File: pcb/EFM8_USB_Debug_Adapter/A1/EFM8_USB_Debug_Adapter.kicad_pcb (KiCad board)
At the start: 2 copper layers, 27 parts, among them J100 EFM8 IDC Debug Header, J101 Conn_01x06, J110 2137160001, J120 31230102, J130 EFM8 USB 8-Bit Debug Header, J131 Conn_01x02_Male, Q110 SI3443CDV-T1-GE3, Q111 DMMT5401, Q120 SI3443CDV-T1-GE3, Q121 DMMT5401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

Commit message: Erstes Layout
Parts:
- removed J101: Conn_01x06, Connector_PinHeader_2.54mm:PinHeader_1x06_P2.54mm_Vertical
- added J111: TTL-232R Header, Connector_PinHeader_2.54mm:PinHeader_1x06_P2.54mm_Vertical, F.Cu at (142.2, 34.3)
- moved D110 47.6 mm to (110.5, 34.3), turned to 180 degrees
- moved R112 47.3 mm to (114.0, 35.0), turned to -90 degrees
- moved R110 45.9 mm to (110.5, 36.8)
- moved F110 44.3 mm to (110.5, 41.9)
- moved R111 43.8 mm to (110.5, 39.4)
- moved D120 39.8 mm to (131.7, 33.9), turned to 90 degrees
- moved R130 38.6 mm to (110.5, 63.5)
- moved J110 38.0 mm to (105.1, 35.1), turned to -90 degrees
- moved R114 33.0 mm to (109.2, 51.0), turned to -90 degrees
- moved R113 31.8 mm to (116.8, 51.0), turned to 90 degrees
- moved Q110 29.9 mm to (111.0, 46.0)
- moved R121 29.3 mm to (124.0, 49.2), turned to 90 degrees
- moved Q111 28.1 mm to (113.0, 51.0), turned to 180 degrees
- moved R120 26.9 mm to (131.7, 39.0), turned to -90 degrees
- moved J131 24.3 mm to (114.3, 58.4), turned to 90 degrees
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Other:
- board outline added: 48 x 35 mm

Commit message: PCB bearbeitet, FreeCAD Projet angelegt
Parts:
- removed J131: Conn_01x02_Male, Connector_PinHeader_2.54mm:PinHeader_1x02_P2.54mm_Vertical
- added D111: 150080SS75000, LED_SMD:LED_0805_2012Metric_Pad1.15x1.40mm_HandSolder, F.Cu at (98.8, 46.8)
- added D121: 150080SS75000, LED_SMD:LED_0805_2012Metric_Pad1.15x1.40mm_HandSolder, F.Cu at (127.8, 34.8)
- added D131: 150080BS75000, LED_SMD:LED_0805_2012Metric_Pad1.15x1.40mm_HandSolder, F.Cu at (98.8, 74.2)
- added JP130: SolderJumper_2_Bridged, Jumper:SolderJumper-2_P1.3mm_Bridged_RoundedPad1.0x1.5mm, F.Cu at (114.0, 58.4)
- added R115: 2k,0603, Resistor_SMD:R_0603_1608Metric_Pad0.98x0.95mm_HandSolder, F.Cu at (107.6, 47.6)
- added R123: 2k,0603, Resistor_SMD:R_0603_1608Metric_Pad0.98x0.95mm_HandSolder, F.Cu at (129.0, 46.8)
- added R133: 2k,0603, Resistor_SMD:R_0603_1608Metric_Pad0.98x0.95mm_HandSolder, F.Cu at (113.2, 67.0)
- D110, D120: value LTST-C191TGKT -> 150080SS75000; footprint LED_SMD:LED_0603_1608Metric_Pad1.05x0.95mm_HandSolder -> LED_SMD:LED_0805_2012Metric_Pad1.15x1.40mm_HandSolder
- D130: value LTST-C191TGKT -> 150080BS75000; footprint LED_SMD:LED_0603_1608Metric_Pad1.05x0.95mm_HandSolder -> LED_SMD:LED_0805_2012Metric_Pad1.15x1.40mm_HandSolder
- F110: value 0805L110SLxx -> 0ZCJ0110FF2E; footprint Fuse:Fuse_0805_2012Metric_Pad1.15x1.40mm_HandSolder -> Fuse:Fuse_1206_3216Metric_Pad1.42x1.75mm_HandSolder
- J100: value EFM8 IDC Debug Header -> EFM8_IDC_Debug_Header_Horizontal; footprint Connector_User:IDC-Header_2x03_P2.54mm_Vertical_61200621621 -> Connector_User:IDC-Header_2x03_P2.54mm_Horizontal_61200621721
- J111: value TTL-232R Header -> TTL-232R_Header_Horizontal; footprint Connector_PinHeader_2.54mm:PinHeader_1x06_P2.54mm_Vertical -> Connector_PinHeader_2.54mm:PinHeader_1x06_P2.54mm_Horizontal
- J130: value EFM8 USB 8-Bit Debug Header -> EFM8_USB_8-Bit_Debug_Header_Horizontal; footprint Connector_User:IDC-Header_2x05_P2.54mm_Vertical_61201021621 -> Connector_User:IDC-Header_2x05_P2.54mm_Horizontal_61201021721
- moved R120 20.8 mm to (111.0, 40.6)
- moved D120 19.5 mm to (112.2, 34.8)
- moved D130 19.5 mm to (98.8, 50.4)
- moved J130 18.6 mm to (108.8, 67.4), turned to 180 degrees
- moved R122 14.4 mm to (118.6, 46.8), turned to -90 degrees
- moved R130 14.0 mm to (107.6, 49.8)
- moved D110 11.7 mm to (98.8, 34.0)
- moved Q120 11.4 mm to (125.2, 52.4)
- moved Q110 10.9 mm to (119.8, 52.4)
- moved R112 7.20 mm to (106.8, 34.8)
- moved Q131 6.56 mm to (117.0, 62.6)
- moved R131 6.56 mm to (120.8, 62.6)
- moved R132 6.56 mm to (113.2, 62.6)
- moved J100 6.48 mm to (134.2, 59.3), turned to 0 degrees
- moved R114 6.24 mm to (113.8, 55.2), turned to 0 degrees
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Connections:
- net Net-(D110-Pad2) renamed /Ext_USB_Power_Fused
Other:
- board size 48 x 35 mm -> 51 x 44 mm

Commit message: Mechanik bearbeitet
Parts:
- moved D121 4.00 mm to (131.8, 34.8)
- moved D120 4.00 mm to (116.2, 34.8)
- moved J100 4.00 mm to (138.2, 59.3)
- moved J111 4.00 mm to (141.4, 35.6)
- moved J120 4.00 mm to (126.5, 41.4)
- moved Q121 4.00 mm to (126.8, 46.8)
- moved R121 4.00 mm to (130.6, 46.8)
- moved R122 4.00 mm to (122.6, 46.8)
- moved R123 4.00 mm to (133.0, 46.8)
- moved R110 1.20 mm to (107.8, 37.8)
- moved R115 1.20 mm to (107.6, 46.4)
- moved R120 1.20 mm to (111.0, 39.4)
- moved F110 1.20 mm to (108.4, 43.6)
- moved R111 1.20 mm to (107.8, 40.6)
- moved R112 1.20 mm to (106.8, 33.6)
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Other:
- board size 51 x 44 mm -> 55 x 45 mm

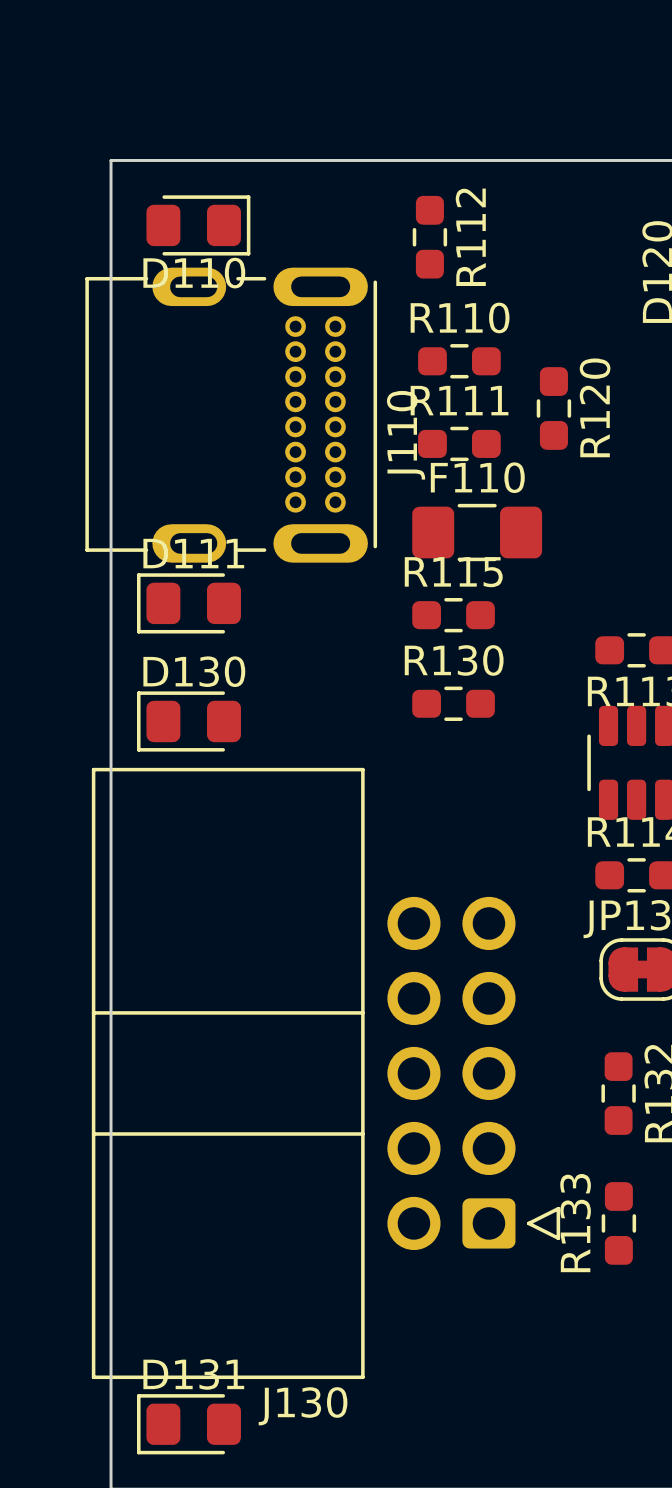
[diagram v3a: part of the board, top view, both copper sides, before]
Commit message: Light Pipes in KiCad hinzugefügt
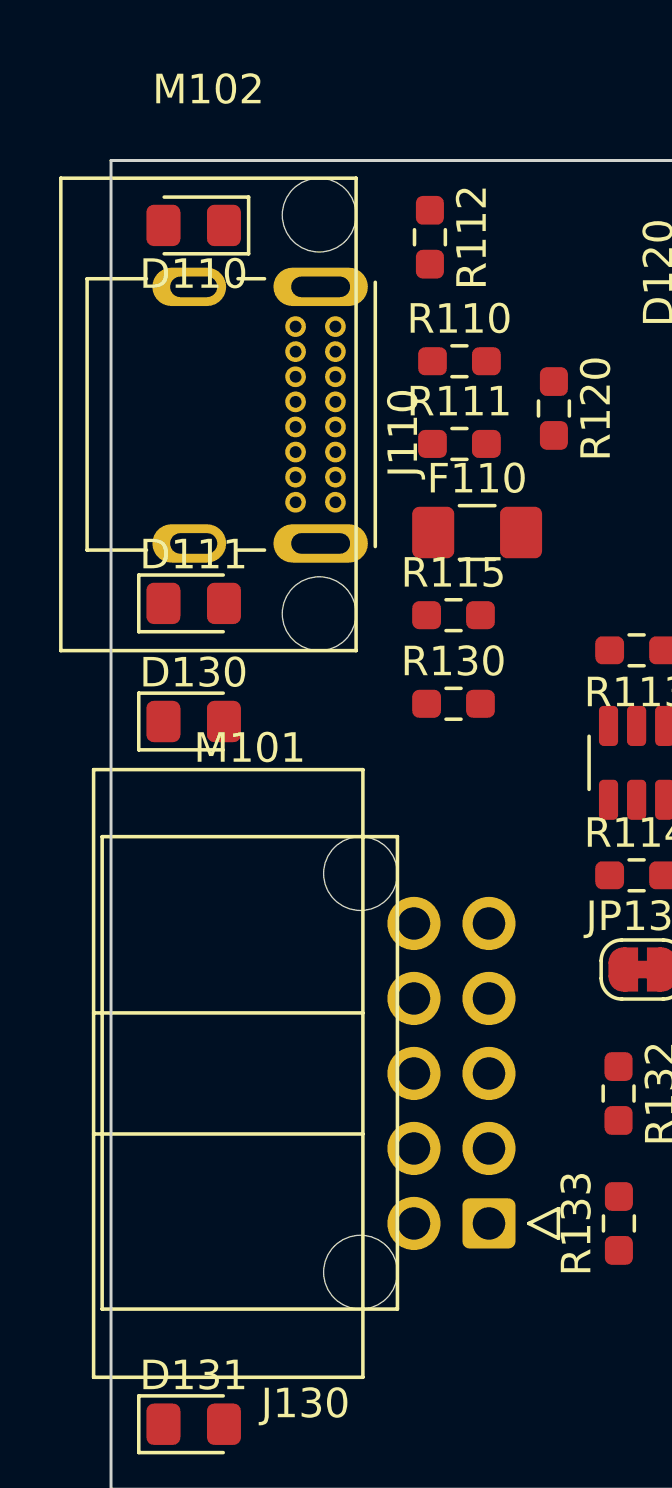
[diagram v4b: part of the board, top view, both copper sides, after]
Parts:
- added M101: DBG8_Light_Pipe, Mechanical_User:DBG8_CON_Light_Pipe, F.Cu at (100.7, 61.9)
- added M102: USB_Light_Pipe, Mechanical_User:USB_CON_Light_Pipe, F.Cu at (99.3, 39.6)
- D130, D131: value 150080BS75000 -> 150080SS75000
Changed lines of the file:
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@@
+    )
+  )
+  (footprint "Mechanical_User:DBG8_CON_Light_Pipe" (layer "F.Cu")
+    (at 100.7 61.9)
+    (property "Sheetfile" "EFM8_USB_Debug_Adapter.kicad_sch")
+    (property "Sheetname" "")
+    (attr through_hole)
+    (fp_text reference "M101" (at 0 -11 unlocked) (layer "F.SilkS")
+      (effects (font (size 1 1) (thickness 0.15)))
+    )
+    (fp_text value "DBG8_Light_Pipe" (at 0 -9 unlocked) (layer "F.Fab")
+      (effects (font (size 1 1) (thickness 0.15)))
+    )
+    (fp_text user "${REFERENCE}" (at 0 -11 unlocked) (layer "F.Fab")
+      (effects (font (size 1 1) (thickness 0.15)))
+    )
+    (fp_line (start -5 -8) (end 5 -8) (layer "F.SilkS") (width 0.12))
+    (fp_line (start 5 8) (end -5 8) (layer "F.SilkS") (width 0.12))
+    (fp_line (start 5 -8) (end 5 8) (layer "F.SilkS") (width 0.12))
+    (fp_line (start -5 8) (end -5 -8) (layer "F.SilkS") (width 0.12))
+    (fp_line (start 0.79 5.48) (end -1.71 5.48) (layer "F.Fab") (width 0.1))
+    (fp_line (start 5 -8) (end 5 8) (layer "F.Fab") (width 0.1))
+    (fp_line (start -1.71 -7.28) (end -1.71 -5.48) (layer "F.Fab") (width 0.1))
+    (fp_line (start 0.79 -5.48) (end 0.79 -7.28) (layer "F.Fab") (width 0.1))
+    (fp_line (start -5 -8) (end 5 -8) (layer "F.Fab") (width 0.1))
+    (fp_line (start 0.79 7.28) (end 0.79 5.48) (layer "F.Fab") (width 0.1))
+    (fp_line (start 5 8) (end -5 8) (layer "F.Fab") (width 0.1))
+    (fp_line (start 0.79 -7.28) (end -1.71 -7.28) (layer "F.Fab") (width 0.1))
+    (fp_line (start -1.71 -5.48) (end 0.79 -5.48) (layer "F.Fab") (width 0.1))
+    (fp_line (start -1.71 7.28) (end 0.79 7.28) (layer "F.Fab") (width 0.1))
+    (fp_line (start -1.71 5.48) (end -1.71 7.28) (layer "F.Fab") (width 0.1))
+    (fp_line (start -5 8) (end -5 -8) (layer "F.Fab") (width 0.1))
+    (pad "" np_thru_hole circle (at 3.75 -6.75) (size 2.5 2.5) (drill 2.5) (layers F&B.Cu *.Mask))
+    (pad "" np_thru_hole circle (at 3.75 6.75) (size 2.5 2.5) (drill 2.5) (layers F&B.Cu *.Mask))
+    (model ":KICAD_3D_USER:Mechanical/USB_CON_Light_Pipe.step"
+      (offset (xyz 24.3 -13.9 0))
+      (scale (xyz 1 1 1))
+      (rotate (xyz 0 0 0))
     )
   )
@@
     (descr "LED SMD 0805 (2012 Metric), square (rectangular) end terminal, IPC_7351 nominal, (Body size source: https://docs.google.com/spreadsheets/d/1BsfQQcO9C6DZCsRaXUlFlo91Tg2WpOkGARC1WS5S8t0/edit?usp=sharing), generated with kicad-footprint-generator")
     (tags "LED handsolder")
-    (property "Info" "Blue")
+    (property "Info" "Red")
     (property "Manufacturer" "Wurth Elektronik")
-    (property "SPN" "732-4982-1-ND")
+    (property "SPN" "732-4985-1-ND")
     (property "Sheetfile" "EFM8_USB_Debug_Adapter.kicad_sch")
     (property "Sheetname" "")
@@
       (effects (font (size 1 1) (thickness 0.15)))
     )
-    (fp_text value "150080BS75000" (at 0 1.65) (layer "F.Fab")
+    (fp_text value "150080SS75000" (at 0 1.65) (layer "F.Fab")
       (effects (font (size 1 1) (thickness 0.15)))
     )
@@
     (model "${KICAD6_3DMODEL_DIR}/LED_SMD.3dshapes/LED_0805_2012Metric.wrl"
       (offset (xyz 0 0 0))
+      (scale (xyz 1 1 1))
+      (rotate (xyz 0 0 0))
+    )
+  )
+  (footprint "Mechanical_User:USB_CON_Light_Pipe" (layer "F.Cu")
+    (at 99.3 39.6)
+    (property "Sheetfile" "EFM8_USB_Debug_Adapter.kicad_sch")
+    (property "Sheetname" "")
+    (attr through_hole)
+    (fp_text reference "M102" (at 0 -11 unlocked) (layer "F.SilkS")
+      (effects (font (size 1 1) (thickness 0.15)))
+    )
+    (fp_text value "USB_Light_Pipe" (at 0 -9 unlocked) (layer "F.Fab")
+      (effects (font (size 1 1) (thickness 0.15)))
+    )
+    (fp_text user "${REFERENCE}" (at 0 -11 unlocked) (layer "F.Fab")
+      (effects (font (size 1 1) (thickness 0.15)))
+    )
+    (fp_line (start 5 8) (end -5 8) (layer "F.SilkS") (width 0.12))
+    (fp_line (start 5 -8) (end 5 8) (layer "F.SilkS") (width 0.12))
+    (fp_line (start -5 8) (end -5 -8) (layer "F.SilkS") (width 0.12))
+    (fp_line (start -5 -8) (end 5 -8) (layer "F.SilkS") (width 0.12))
+    (fp_line (start -1.71 -7.48) (end -1.71 -5.68) (layer "F.Fab") (width 0.1))
+    (fp_line (start -5 8) (end -5 -8) (layer "F.Fab") (width 0.1))
+    (fp_line (start 5 -8) (end 5 8) (layer "F.Fab") (width 0.1))
+    (fp_line (start -5 -8) (end 5 -8) (layer "F.Fab") (width 0.1))
+    (fp_line (start 5 8) (end -5 8) (layer "F.Fab") (width 0.1))
+    (fp_line (start -5 -5.48) (end 5 -5.48) (layer "F.Fab") (width 0.1))
+    (fp_line (start -5 5.53) (end 5 5.53) (layer "F.Fab") (width 0.1))
+    (fp_line (start -1.71 -5.68) (end 0.79 -5.68) (layer "F.Fab") (width 0.1))
+    (fp_line (start 0.79 7.48) (end 0.79 5.68) (layer "F.Fab") (width 0.1))
+    (fp_line (start -1.71 7.48) (end 0.79 7.48) (layer "F.Fab") (width 0.1))
+    (fp_line (start 0.79 -5.68) (end 0.79 -7.48) (layer "F.Fab") (width 0.1))
+    (fp_line (start 0.79 5.68) (end -1.71 5.68) (layer "F.Fab") (width 0.1))
+    (fp_line (start -1.71 5.68) (end -1.71 7.48) (layer "F.Fab") (width 0.1))
+    (fp_line (start 0.79 -7.48) (end -1.71 -7.48) (layer "F.Fab") (width 0.1))
+    (pad "" np_thru_hole circle (at 3.75 -6.75) (size 2.5 2.5) (drill 2.5) (layers F&B.Cu *.Mask))
+    (pad "" np_thru_hole circle (at 3.75 6.75) (size 2.5 2.5) (drill 2.5) (layers F&B.Cu *.Mask))
+    (model ":KICAD_3D_USER:Mechanical/USB_CON_Light_Pipe.step"
+      (offset (xyz 24.3 -13.9 0))
       (scale (xyz 1 1 1))
       (rotate (xyz 0 0 0))
@@
     (descr "LED SMD 0805 (2012 Metric), square (rectangular) end terminal, IPC_7351 nominal, (Body size source: https://docs.google.com/spreadsheets/d/1BsfQQcO9C6DZCsRaXUlFlo91Tg2WpOkGARC1WS5S8t0/edit?usp=sharing), generated with kicad-footprint-generator")
     (tags "LED handsolder")
-    (property "Info" "Blue")
+    (property "Info" "Red")
     (property "Manufacturer" "Wurth Elektronik")
-    (property "SPN" "732-4982-1-ND")
+    (property "SPN" "732-4985-1-ND")
     (property "Sheetfile" "EFM8_USB_Debug_Adapter.kicad_sch")
     (property "Sheetname" "")
@@
       (effects (font (size 1 1) (thickness 0.15)))
     )
-    (fp_text value "150080BS75000" (at 0 1.65) (layer "F.Fab")
-      (effects (font (size 1 1) (thickness 0.15)))
-    )
+    (fp_text value "150080SS75000" (at 0 1.65) (layer "F.Fab")
+      (effects (font (size 1 1) (thickness 0.15)))
+    )

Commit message: Lightpipes aktualisiert
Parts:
- added M120: PSU_Light_Pipe, Mechanical_User:PSU_CON_Light_Pipe, F.Cu at (124.0, 35.5)
- moved J120 1.60 mm to (126.5, 39.8)
- moved M110 0.77 mm to (100.1, 39.6), turned to -90 degrees
- moved M130 0.71 mm to (100.0, 62.0), turned to -90 degrees
- renumbered M102 to M110, M101 to M130

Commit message: PCB bearbeitet
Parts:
- removed JP130: SolderJumper_2_Bridged, Jumper:SolderJumper-2_P1.3mm_Bridged_RoundedPad1.0x1.5mm
- added J131: Header_01x02_Wurth_61300211121, Connector_PinHeader_2.54mm:PinHeader_1x02_P2.54mm_Vertical, F.Cu at (116.7, 58.5)
- moved R133 9.12 mm to (107.6, 74.2), turned to 0 degrees
- moved Q131 5.61 mm to (122.5, 63.7)
- moved R131 5.61 mm to (126.3, 63.7)
- moved R132 5.61 mm to (118.7, 63.7)
- moved Q130 2.79 mm to (122.5, 58.5)
- moved R113 1.73 mm to (114.1, 45.9)
- moved R114 1.73 mm to (114.1, 53.5)
- moved Q111 1.73 mm to (114.1, 49.7)
- moved R120 1.10 mm to (112.1, 39.3)
- moved D130 0.78 mm to (99.5, 50.2), turned to 180 degrees
- moved D111 0.76 mm to (99.5, 45.9), turned to 180 degrees
- moved D110 0.76 mm to (99.5, 33.3)
- moved D131 0.75 mm to (99.5, 73.8), turned to 180 degrees
- moved R112 0.50 mm to (106.8, 34.1)
- moved R130 0.50 mm to (107.6, 49.9)
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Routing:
- net Net-(D130-Pad2): track 0.00 -> 69.1 mm
- net /Ext_USB_Power_Fused: track 0.00 -> 63.1 mm
- net /V_PROG: track 0.00 -> 55.9 mm, vias 0 -> 2
- net Net-(D110-Pad1): track 0.00 -> 53.3 mm, vias 0 -> 2
- net /C2D: track 0.00 -> 42.7 mm
- net /Ext_PSU_Power: track 0.00 -> 42.6 mm
- net /C2CK: track 0.00 -> 39.7 mm
- net Net-(J110-PadB5): track 0.00 -> 28.6 mm, vias 0 -> 1
- net /UART_RX: track 0.00 -> 27.1 mm
- net /UART_TX: track 0.00 -> 24.4 mm
- net Net-(Q120-Pad3): track 0.00 -> 13.5 mm, vias 0 -> 2
- net Net-(D121-Pad1): track 0.00 -> 13.1 mm
- net /Ext_USB_Power: track 0.00 -> 13.0 mm
- net /Prog_USB_Power: track 0.00 -> 11.3 mm
- net Net-(Q110-Pad3): track 0.00 -> 9.96 mm
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- added copper zone on B.Cu, net GND
- added copper zone on F.Cu, net GND

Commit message: Stecker verschoben
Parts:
- moved J111 1.10 mm to (142.4, 35.6)
- moved J100 1.10 mm to (139.5, 59.3)
- moved J130 0.90 mm to (107.5, 67.0)
- moved D110 0.80 mm to (98.8, 33.3)
- moved D111 0.80 mm to (98.8, 45.9)
- moved D120 0.80 mm to (116.2, 33.8)
- moved D121 0.80 mm to (131.8, 33.8)
- moved D130 0.80 mm to (98.8, 50.2)
- moved D131 0.80 mm to (98.8, 73.8)
- moved J120 0.80 mm to (126.5, 39.3)
- moved M110 0.80 mm to (99.2, 39.6)
- moved M120 0.80 mm to (124.0, 34.5)
- moved M130 0.80 mm to (99.2, 62.0)
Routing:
- net /Ext_USB_Power_Fused: track 63.1 -> 61.6 mm
- net /C2D: track 42.7 -> 43.9 mm
- net /C2CK: track 39.7 -> 40.8 mm
- net Net-(D130-Pad1): track 9.79 -> 10.7 mm
- net /Ext_PSU_Power: track 42.6 -> 43.4 mm
- net Net-(D130-Pad2): track 69.1 -> 68.6 mm
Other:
- board text added: "EFM8 USB Debug Adapter Rev. A1"
- board text added: "GND"
- board text added: "Prog_USB_Power"
- board text added: "RX"
- board text added: "TX"

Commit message: PCB Rev. A1
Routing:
- net /V_PROG: track 55.9 -> 57.0 mm
